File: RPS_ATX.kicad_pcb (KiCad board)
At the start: 2 copper layers, 100 x 50 mm, 71 parts, among them J1 494_ON, J10 MCU_FAN, J11 PW_IN, J13 FAN_OUT, J2 494_OUT, J3 POT, J5 PS_OUT-, J6 PS_OUT+, J7 RPS_OUT-, J8 MEAS, J9 RPS_OUT+, Q2 AO3400A, Q3 AO3400A, U1 TL494, U2 Mini360, U4 TL431DBZ, U5 LM358, U6 INA226, U7 LM7805_TO220

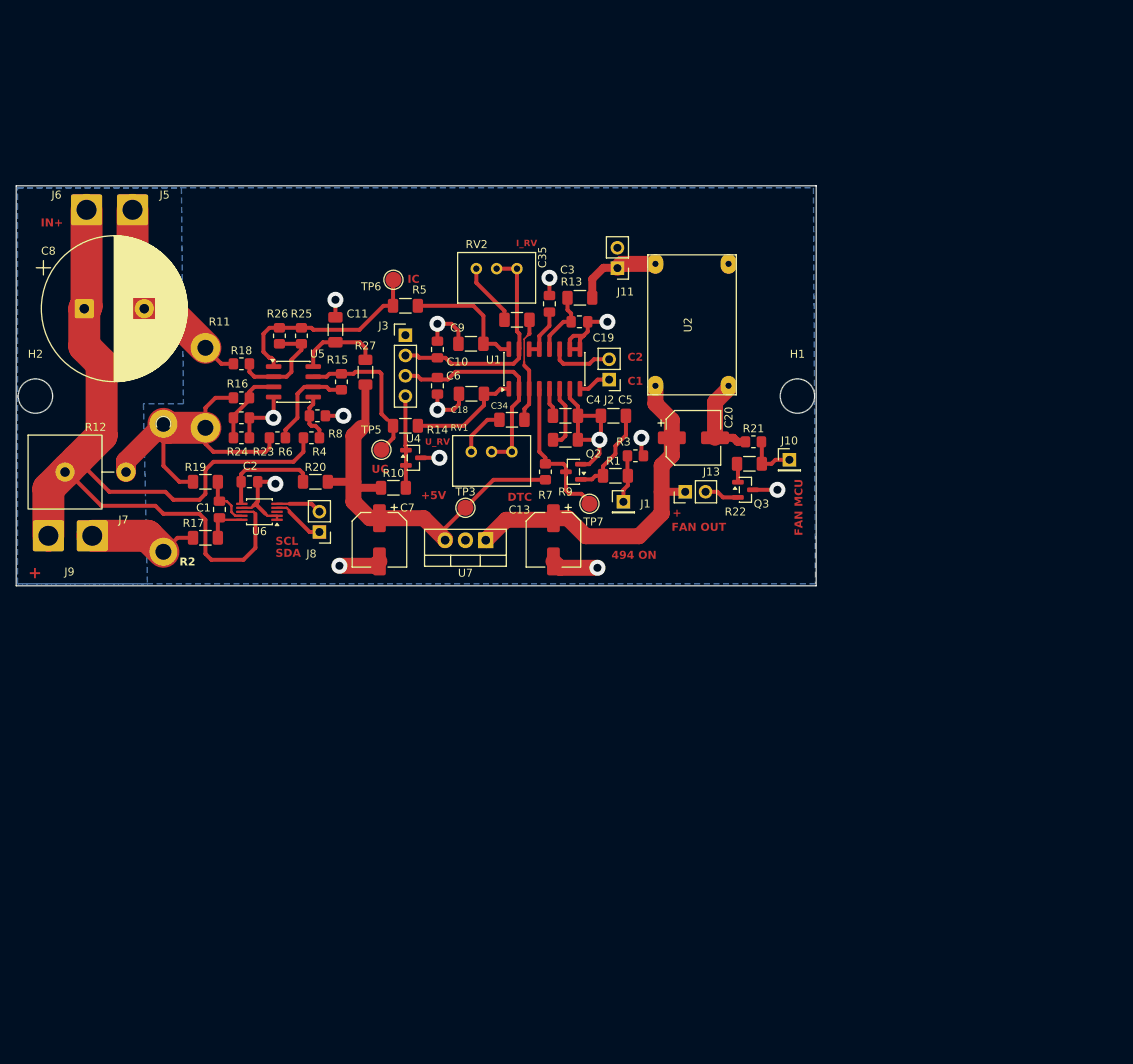
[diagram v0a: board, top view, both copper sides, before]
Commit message: changed OpAmp resistor values for i channel, top layer gnd filled zone
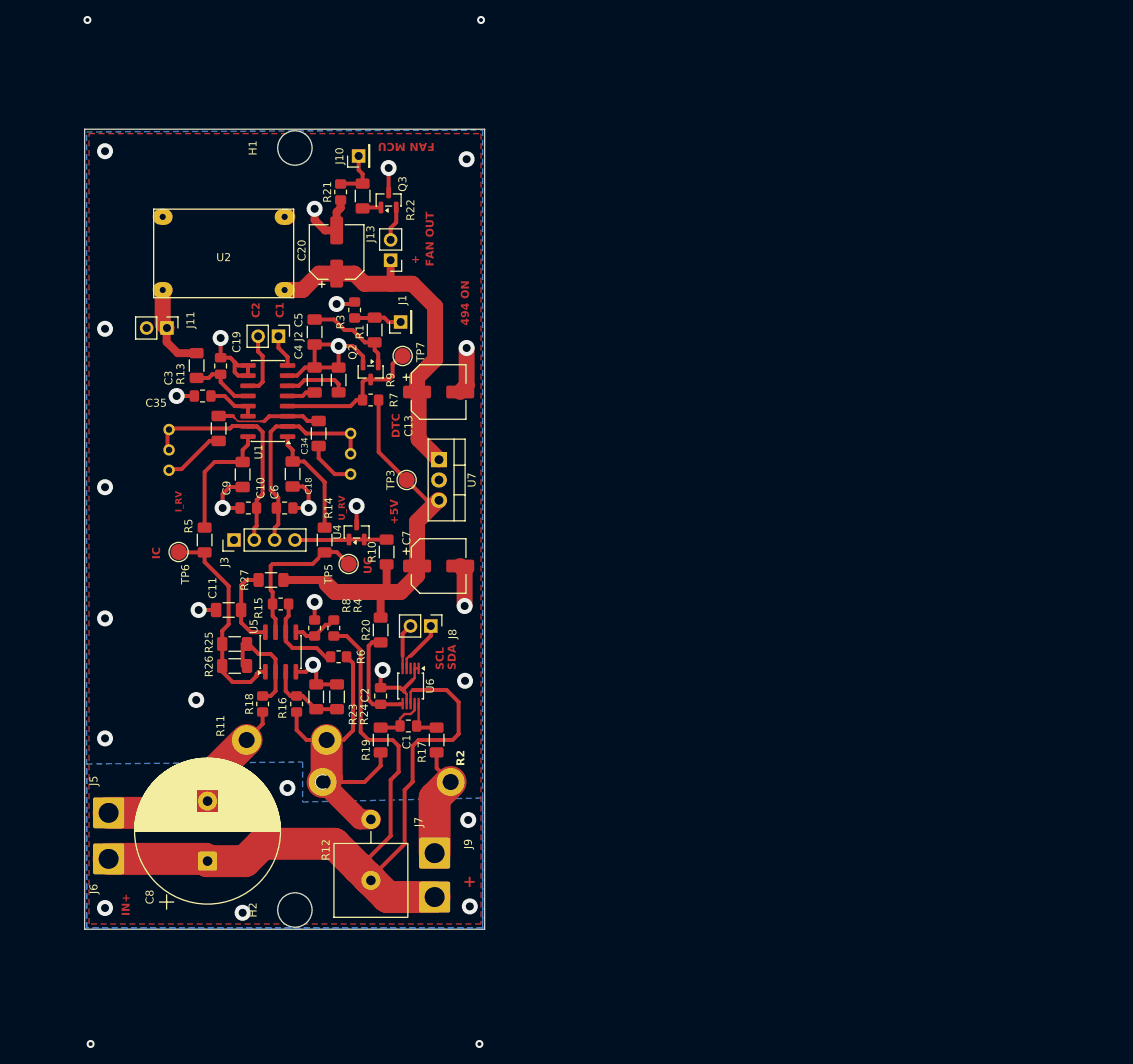
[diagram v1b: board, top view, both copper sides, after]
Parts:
- R23, R24, R25, R26: value 10K 0.01% -> 100K 0.01%; footprint Resistor_SMD:R_0805_2012Metric_Pad1.20x1.40mm_HandSolder -> Resistor_SMD:R_1206_3216Metric_Pad1.30x1.75mm_HandSolder
- RV1, RV2: moved to B.Cu
- moved J6 81.2 mm to (65.9, 139.4), turned to 90 degrees
- moved J5 75.4 mm to (65.9, 133.6), turned to 90 degrees
- moved H2 72.0 mm to (89.2, 145.8), turned to 90 degrees
- moved C8 70.8 mm to (78.3, 139.7), turned to 90 degrees
- moved H1 70.1 mm to (89.2, 50.5), turned to 90 degrees
- moved J9 66.1 mm to (106.7, 144.2), turned to 90 degrees
- moved J10 65.9 mm to (97.2, 51.5), turned to 90 degrees
- moved R12 63.8 mm to (98.7, 142.1), turned to 90 degrees
- moved R21 60.3 mm to (94.9, 56.0), turned to 90 degrees
- moved U2 59.2 mm to (80.3, 63.7), turned to 0 degrees
- moved R22 58.8 mm to (97.7, 56.5), turned to -90 degrees
- moved J7 58.4 mm to (106.7, 138.7), turned to 90 degrees
- moved Q3 57.5 mm to (100.9, 57.0), turned to 90 degrees
- moved J11 56.8 mm to (73.2, 73.0), turned to -90 degrees
- moved C20 50.3 mm to (94.4, 63.5), turned to 90 degrees
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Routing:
- net GND: track 126.4 -> 123.8 mm, vias 14 -> 28
- net MEAS_I+: track 42.2 -> 43.7 mm
- net Net-(U5B--): track 12.1 -> 11.1 mm
- net VOUT: track 118.4 -> 119.2 mm
- net (no net): vias 0 -> 4
- added copper zone on F.Cu, net GND
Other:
- board size 100 x 50 mm -> 50 x 100 mm

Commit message: rectified wrong fan transistor connection
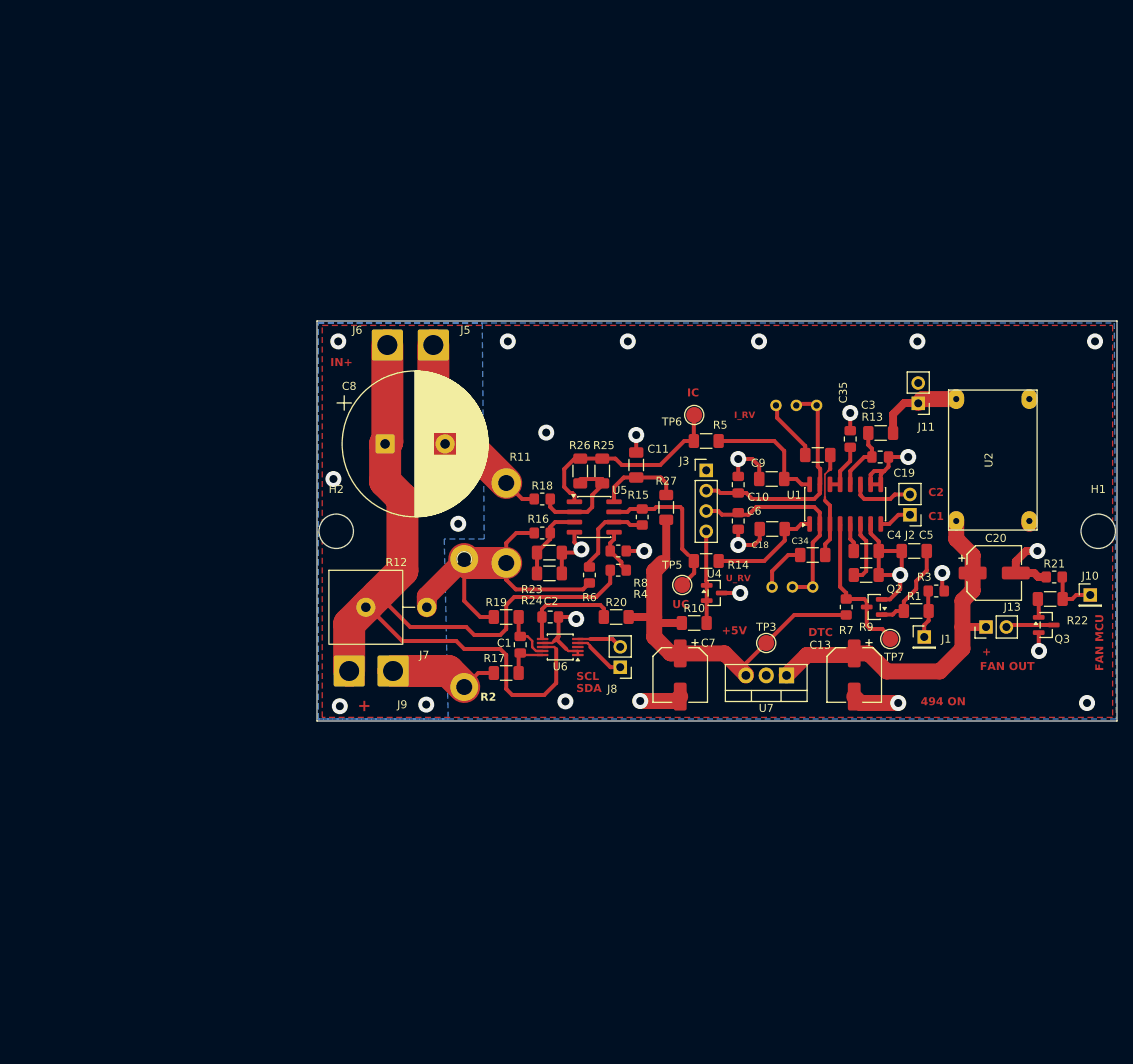
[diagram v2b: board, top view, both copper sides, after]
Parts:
- moved H1 111.3 mm to (189.6, 98.4), turned to 0 degrees
- moved J10 106.7 mm to (188.6, 106.4), turned to 0 degrees
- moved R21 101.4 mm to (184.1, 104.2), turned to 0 degrees
- moved R22 99.6 mm to (183.6, 106.9), turned to 180 degrees
- moved U2 99.5 mm to (176.4, 89.5), turned to -90 degrees
- moved Q3 97.9 mm to (183.1, 110.2), turned to 0 degrees
- moved J11 94.4 mm to (167.1, 82.4), turned to 180 degrees
- moved C20 91.5 mm to (176.6, 103.7), turned to 0 degrees
- moved J13 87.4 mm to (175.6, 110.4), turned to 90 degrees
- moved R13 85.9 mm to (162.4, 86.2), turned to 180 degrees
- moved C19 83.2 mm to (162.3, 89.2), turned to 0 degrees
- moved J2 82.0 mm to (166.1, 96.4), turned to 180 degrees
- moved C3 81.1 mm to (158.6, 86.9), turned to 90 degrees
- moved RV2 81.0 mm to (154.4, 82.7), turned to 0 degrees
- moved R3 80.7 mm to (169.3, 105.9), turned to 180 degrees
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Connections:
- J13 pad 2: /fan- -> Net-(J13-Pin_2)
- Q3 pad 2: /fan- -> GND
- Q3 pad 3: GND -> Net-(J13-Pin_2)
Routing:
- net Net-(J13-Pin_2): track 0.00 -> 6.03 mm
- net /fan-: track 4.34 -> 0.00 mm
- net GND: track 123.8 -> 123.1 mm
- net (no net): vias 4 -> 0
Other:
- board size 50 x 100 mm -> 100 x 50 mm

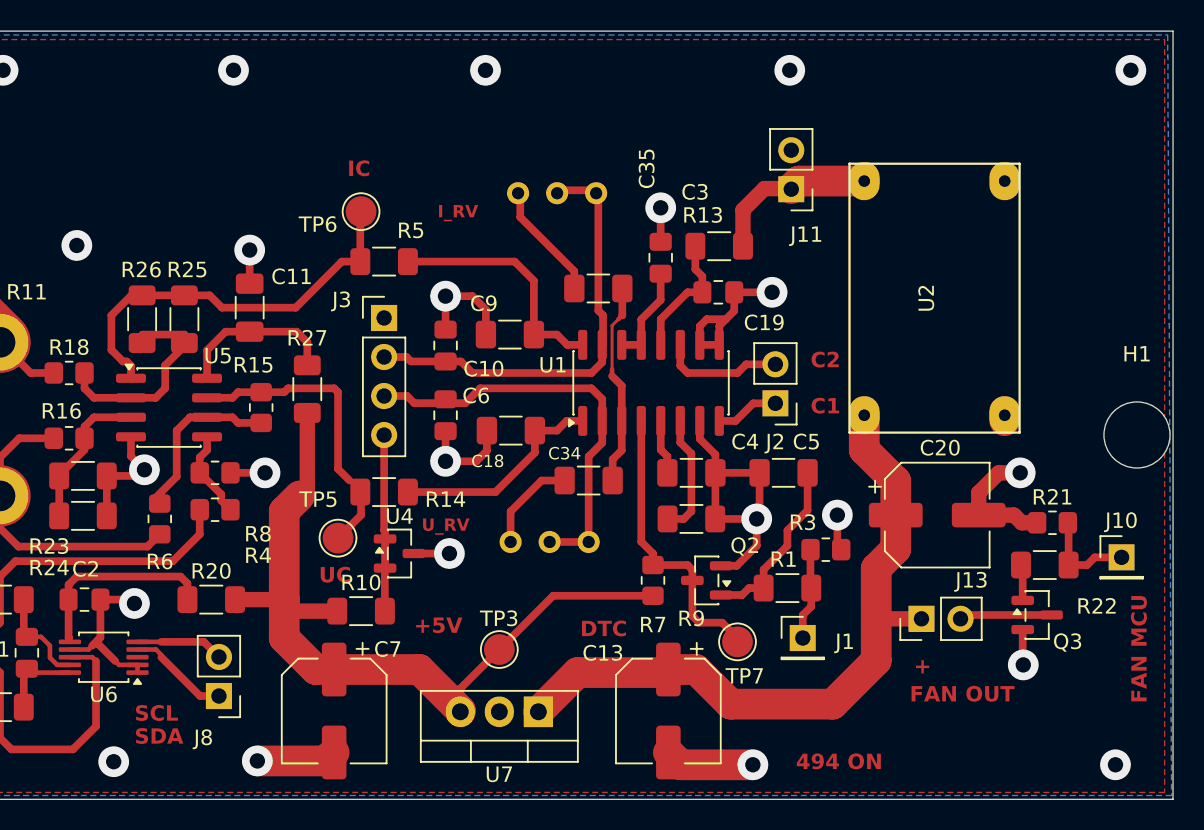
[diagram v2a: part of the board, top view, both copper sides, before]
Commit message: added: fuse(+17V), C(+17V) , INA226 pullup resistors
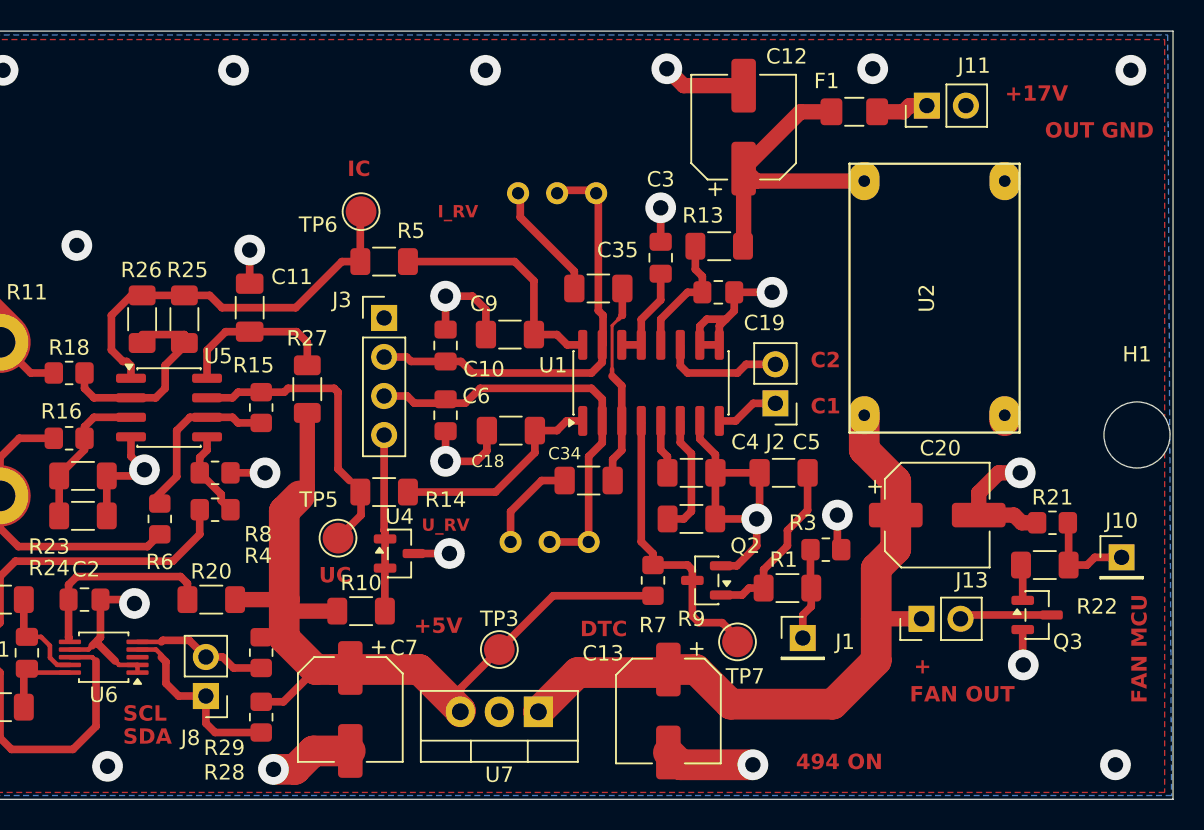
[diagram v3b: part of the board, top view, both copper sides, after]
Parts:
- added C12: 100uF, Capacitor_SMD:CP_Elec_6.3x5.4_Nichicon, F.Cu at (164.0, 78.4)
- added F1: 0.5A, Fuse:Fuse_1206_3216Metric_Pad1.42x1.75mm_HandSolder, F.Cu at (171.2, 77.4)
- added R28: 5.1K, Resistor_SMD:R_0805_2012Metric_Pad1.20x1.40mm_HandSolder, F.Cu at (132.6, 116.8)
- added R29: 5.1K, Resistor_SMD:R_0805_2012Metric_Pad1.20x1.40mm_HandSolder, F.Cu at (132.6, 112.6)
- moved J11 10.4 mm to (175.9, 77.0), turned to 90 degrees
- moved C7 1.05 mm to (138.4, 116.3)
- moved J8 0.85 mm to (129.0, 115.4)
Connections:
- net Net-(J13-Pin_2) renamed /fan-
- J11 pad 1: +17.5V_ATX -> Net-(J11-Pin_1)
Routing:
- net +17.5V_ATX: track 11.0 -> 20.5 mm
- net GND: track 123.1 -> 128.8 mm, vias 28 -> 29
- net Net-(J8-Pin_1): track 6.64 -> 12.2 mm
- net +5V: track 52.3 -> 56.7 mm
- net Net-(J11-Pin_1): track 0.00 -> 3.40 mm
- net Net-(J8-Pin_2): track 5.71 -> 8.84 mm
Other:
- board text added: "+17V"
- board text added: "OUT GND"

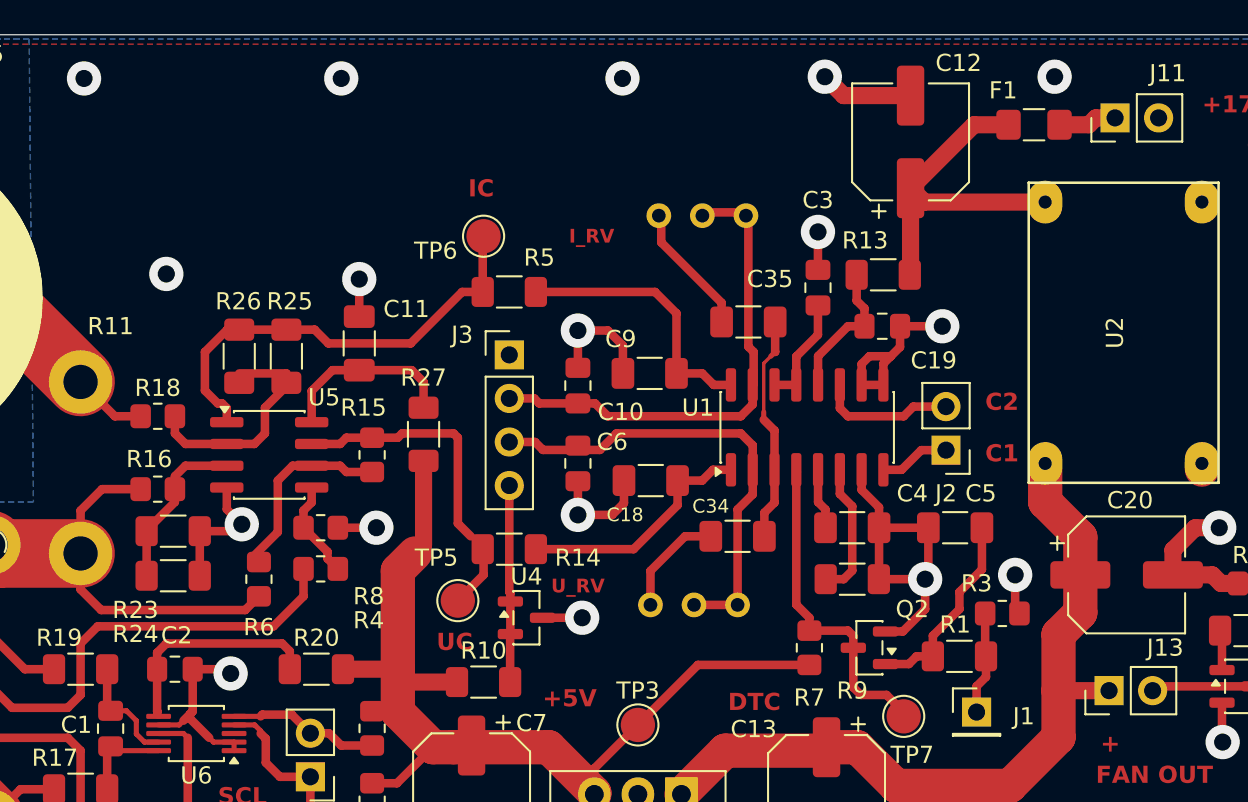
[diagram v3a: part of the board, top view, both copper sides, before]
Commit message: ref voltage from 2.5 to 5 V
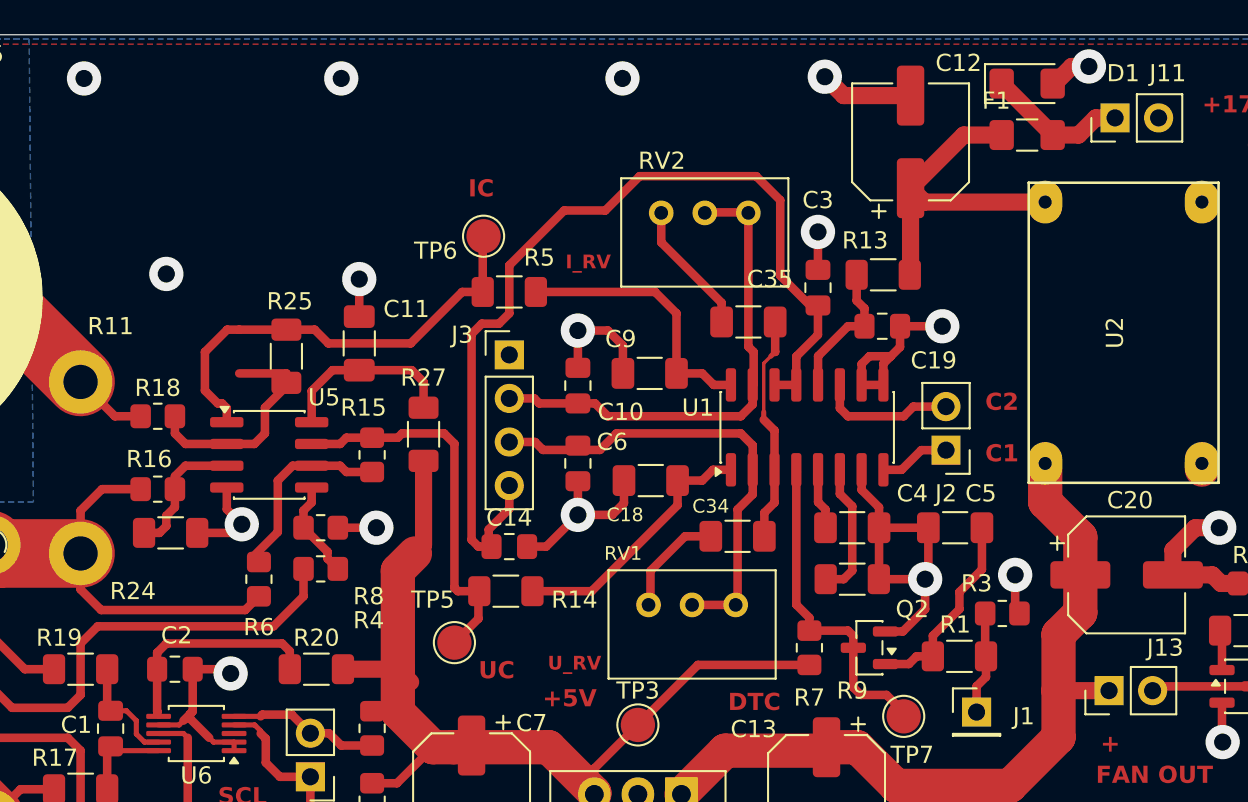
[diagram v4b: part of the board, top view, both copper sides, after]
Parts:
- removed R10: 1K, Resistor_SMD:R_1206_3216Metric_Pad1.30x1.75mm_HandSolder
- removed R23, R26: 100K 0.01%, Resistor_SMD:R_1206_3216Metric_Pad1.30x1.75mm_HandSolder
- removed U4: TL431DBZ, Package_TO_SOT_SMD:SOT-23
- added C14: 100n, Capacitor_SMD:C_0805_2012Metric_Pad1.18x1.45mm_HandSolder, F.Cu at (140.6, 102.0)
- added D1: D, Diode_SMD:D_1206_3216Metric_Pad1.42x1.75mm_HandSolder, F.Cu at (170.8, 75.0)
- C34: value 33n -> 22n
- C35: value 22n -> 33n
- R15, R8: value 1K 0.01% -> 1.8K 0.01%
- RV1, RV2: moved to F.Cu
- moved R24 2.50 mm to (120.8, 101.2)
- moved R14 2.46 mm to (140.4, 104.6)
- moved TP5 2.46 mm to (137.4, 107.6)
- moved F1 0.72 mm to (170.8, 78.0)
- moved RV2 0.21 mm to (154.5, 82.5)
- moved RV1 0.11 mm to (153.8, 105.4)
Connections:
- J11 pad 2: GND -> unconnected-(J11-Pin_2-Pad2)
- J3 pad 4: +2V5 -> +5V_REF
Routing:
- net +5V_REF: track 6.43 -> 55.2 mm
- net +2V5: track 11.5 -> 0.00 mm
- net Net-(D1-K): track 3.40 -> 8.28 mm
- net Net-(R14-Pad1): track 18.6 -> 22.4 mm
- net +5V: track 56.7 -> 54.0 mm
- net /Analog/sh_meas_r+: track 9.76 -> 7.85 mm
- net GND: track 128.8 -> 130.3 mm, vias 29 -> 28
- net U_1IN+: track 14.1 -> 15.4 mm
- net +17.5V_ATX: track 20.5 -> 19.9 mm
